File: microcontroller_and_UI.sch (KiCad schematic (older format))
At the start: 36 parts

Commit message: Annotate schematic symbols
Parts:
- gave numbers to parts that had none: 36

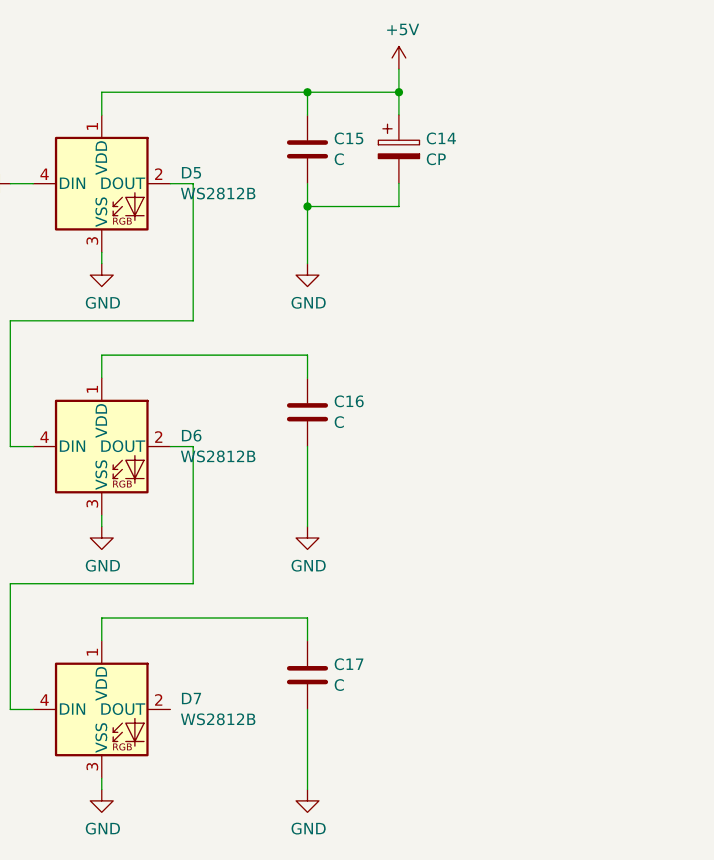
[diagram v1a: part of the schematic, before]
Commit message: Assign PCB footprints
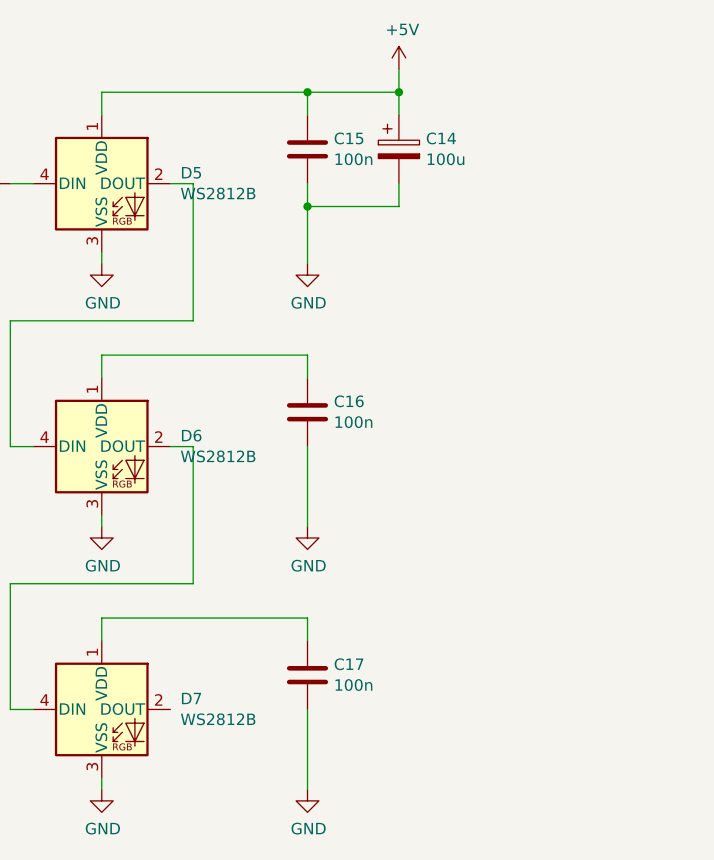
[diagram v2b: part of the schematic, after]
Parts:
- BZ1: footprint (none) -> Library:Buzzer_13.8x6.8RM7.6
- C10, C11, C12, C13, C7, C8, C9: footprint (none) -> Library:C_1206
- C14: value CP -> 100u; footprint (none) -> Library:CP_Elec_6.3x5.8
- C15, C16, C17: value C -> 100n; footprint (none) -> Library:C_1206
- C6: footprint (none) -> Library:CP_2312
- D2, D4: footprint (none) -> Library:LED_0805
- D5, D6, D7: footprint LED_SMD:LED_WS2812B_PLCC4_5.0x5.0mm_P3.2mm -> Library:LED_WS2812B
- D8: footprint (none) -> Library:D_SOD-80
- L2: footprint (none) -> Library:L_TDK_NLC453232
- Q2: footprint Package_TO_SOT_SMD:SOT-23 -> Library:SOT-23
- R10, R11, R12, R13, R14, R15, R16, R6, R7, R8, R9: footprint (none) -> Library:R_1206
- SW2, SW3: footprint (none) -> Library:SW_Push_CK_KMR2
- U3: footprint Package_QFP:TQFP-44_10x10mm_P0.8mm -> Library:TQFP-44
- Y1: footprint (none) -> Library:Crystal_HC49US
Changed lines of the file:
@@
 F 0 "U3" H 3450 3150 50  0000 C CNN
 F 1 "ATmega324PB-AU" H 3450 3050 50  0000 C CNN
-F 2 "Package_QFP:TQFP-44_10x10mm_P0.8mm" H 3900 4700 50  0001 C CIN
+F 2 "Library:TQFP-44" H 3900 4700 50  0001 C CIN
 F 3 "http://ww1.microchip.com/downloads/en/DeviceDoc/40001908A.pdf" H 3900 4700 50  0001 C CNN
 	1    3900 4700
@@
 F 0 "C7" H 1915 1496 50  0000 L CNN
 F 1 "100n" H 1915 1405 50  0000 L CNN
-F 2 "" H 1838 1300 50  0001 C CNN
+F 2 "Library:C_1206" H 1838 1300 50  0001 C CNN
 F 3 "~" H 1800 1450 50  0001 C CNN
 	1    1800 1450
@@
 F 0 "L2" H 2252 1496 50  0000 L CNN
 F 1 "10u" H 2252 1405 50  0000 L CNN
-F 2 "" H 2200 1450 50  0001 C CNN
+F 2 "Library:L_TDK_NLC453232" H 2200 1450 50  0001 C CNN
 F 3 "~" H 2200 1450 50  0001 C CNN
 	1    2200 1450
@@
 F 0 "C8" H 2315 1896 50  0000 L CNN
 F 1 "100n" H 2315 1805 50  0000 L CNN
-F 2 "" H 2238 1700 50  0001 C CNN
+F 2 "Library:C_1206" H 2238 1700 50  0001 C CNN
 F 3 "~" H 2200 1850 50  0001 C CNN
 	1    2200 1850
@@
 F 0 "C6" H 1518 1496 50  0000 L CNN
 F 1 "10u" H 1518 1405 50  0000 L CNN
-F 2 "" H 1438 1300 50  0001 C CNN
+F 2 "Library:CP_2312" H 1438 1300 50  0001 C CNN
 F 3 "~" H 1400 1450 50  0001 C CNN
 	1    1400 1450
@@
 F 0 "D8" V 2154 3230 50  0000 L CNN
 F 1 "D" V 2245 3230 50  0000 L CNN
-F 2 "" H 2200 3150 50  0001 C CNN
+F 2 "Library:D_SOD-80" H 2200 3150 50  0001 C CNN
 F 3 "~" H 2200 3150 50  0001 C CNN
 	1    2200 3150
@@
 F 0 "R7" H 1870 3196 50  0000 L CNN
 F 1 "4k7" H 1870 3105 50  0000 L CNN
-F 2 "" V 1730 3150 50  0001 C CNN
+F 2 "Library:R_1206" V 1730 3150 50  0001 C CNN
 F 3 "~" H 1800 3150 50  0001 C CNN
 	1    1800 3150
@@
 F 0 "C9" H 1915 4296 50  0000 L CNN
 F 1 "100n" H 1915 4205 50  0000 L CNN
-F 2 "" H 1838 4100 50  0001 C CNN
+F 2 "Library:C_1206" H 1838 4100 50  0001 C CNN
 F 3 "~" H 1800 4250 50  0001 C CNN
 	1    1800 4250
@@
 F 0 "SW2" V 1354 3848 50  0000 L CNN
 F 1 "SW_Push" V 1445 3848 50  0000 L CNN
-F 2 "" H 1400 3900 50  0001 C CNN
+F 2 "Library:SW_Push_CK_KMR2" H 1400 3900 50  0001 C CNN
 F 3 "~" H 1400 3900 50  0001 C CNN
 	1    1400 3700
@@
 F 0 "R6" H 1470 4296 50  0000 L CNN
 F 1 "330R" H 1470 4205 50  0000 L CNN
-F 2 "" V 1330 4250 50  0001 C CNN
+F 2 "Library:R_1206" V 1330 4250 50  0001 C CNN
 F 3 "~" H 1400 4250 50  0001 C CNN
 	1    1400 4250
@@
 F 0 "C10" V 2298 4100 50  0000 C CNN
 F 1 "22p" V 2389 4100 50  0000 C CNN
-F 2 "" H 2588 3950 50  0001 C CNN
+F 2 "Library:C_1206" H 2588 3950 50  0001 C CNN
 F 3 "~" H 2550 4100 50  0001 C CNN
 	1    2550 4100
@@
 F 0 "C11" V 2298 4400 50  0000 C CNN
 F 1 "22p" V 2389 4400 50  0000 C CNN
-F 2 "" H 2588 4250 50  0001 C CNN
+F 2 "Library:C_1206" H 2588 4250 50  0001 C CNN
 F 3 "~" H 2550 4400 50  0001 C CNN
 	1    2550 4400
@@
 F 0 "Y1" V 2754 4381 50  0000 L CNN
 F 1 "Crystal" V 2845 4381 50  0000 L CNN
-F 2 "" H 2800 4250 50  0001 C CNN
+F 2 "Library:Crystal_HC49US" H 2800 4250 50  0001 C CNN
 F 3 "~" H 2800 4250 50  0001 C CNN
 	1    2800 4250
@@
 F 0 "C12" H 2665 4996 50  0000 L CNN
 F 1 "100n" H 2665 4905 50  0000 L CNN
-F 2 "" H 2588 4800 50  0001 C CNN
+F 2 "Library:C_1206" H 2588 4800 50  0001 C CNN
 F 3 "~" H 2550 4950 50  0001 C CNN
 	1    2550 4950
@@
 F 0 "R8" H 4570 1496 50  0000 L CNN
 F 1 "4k7" H 4570 1405 50  0000 L CNN
-F 2 "" V 4430 1450 50  0001 C CNN
+F 2 "Library:R_1206" V 4430 1450 50  0001 C CNN
 F 3 "~" H 4500 1450 50  0001 C CNN
 	1    4500 1450
@@
 F 0 "R9" H 4570 1896 50  0000 L CNN
 F 1 "7k5" H 4570 1805 50  0000 L CNN
-F 2 "" V 4430 1850 50  0001 C CNN
+F 2 "Library:R_1206" V 4430 1850 50  0001 C CNN
 F 3 "~" H 4500 1850 50  0001 C CNN
 	1    4500 1850
@@
 F 0 "R11" H 7120 5446 50  0000 L CNN
 F 1 "1k" H 7120 5355 50  0000 L CNN
-F 2 "" V 6980 5400 50  0001 C CNN
+F 2 "Library:R_1206" V 6980 5400 50  0001 C CNN
 F 3 "~" H 7050 5400 50  0001 C CNN
 	1    7050 5400
@@
 F 0 "R10" H 6070 5446 50  0000 L CNN
 F 1 "1k" H 6070 5355 50  0000 L CNN
-F 2 "" V 5930 5400 50  0001 C CNN
+F 2 "Library:R_1206" V 5930 5400 50  0001 C CNN
 F 3 "~" H 6000 5400 50  0001 C CNN
 	1    6000 5400
@@
 F 0 "D4" V 7089 5782 50  0000 R CNN
 F 1 "YELLOW LED" V 6998 5782 50  0000 R CNN
-F 2 "" H 7050 5900 50  0001 C CNN
+F 2 "Library:LED_0805" H 7050 5900 50  0001 C CNN
 F 3 "~" H 7050 5900 50  0001 C CNN
 	1    7050 5900
@@
 F 0 "D2" V 6039 5782 50  0000 R CNN
 F 1 "GREEN LED" V 5948 5782 50  0000 R CNN
-F 2 "" H 6000 5900 50  0001 C CNN
+F 2 "Library:LED_0805" H 6000 5900 50  0001 C CNN
 F 3 "~" H 6000 5900 50  0001 C CNN
 	1    6000 5900
@@
 F 0 "BZ1" H 9655 5690 50  0000 C CNN
 F 1 "Buzzer" H 9655 5599 50  0000 C CNN
-F 2 "" V 9625 5500 50  0001 C CNN
+F 2 "Library:Buzzer_13.8x6.8RM7.6" V 9625 5500 50  0001 C CNN
 F 3 "~" V 9625 5500 50  0001 C CNN
 	1    9650 5400
@@
 F 0 "R15" V 10043 5950 50  0000 C CNN
 F 1 "10k" V 10134 5950 50  0000 C CNN
-F 2 "" V 10180 5950 50  0001 C CNN
+F 2 "Library:R_1206" V 10180 5950 50  0001 C CNN
 F 3 "~" H 10250 5950 50  0001 C CNN
 	1    10250 5950
@@
 F 0 "R14" H 10120 5446 50  0000 L CNN
 F 1 "10k" H 10120 5355 50  0000 L CNN
-F 2 "" V 9980 5400 50  0001 C CNN
+F 2 "Library:R_1206" V 9980 5400 50  0001 C CNN
 F 3 "~" H 10050 5400 50  0001 C CNN
 	1    10050 5400
@@
 F 0 "Q2" H 10055 5996 50  0000 L CNN
 F 1 "BSS138" H 10055 5905 50  0000 L CNN
-F 2 "Package_TO_SOT_SMD:SOT-23" H 10050 5875 50  0001 L CIN
+F 2 "Library:SOT-23" H 10050 5875 50  0001 L CIN
 F 3 "https://www.onsemi.com/pub/Collateral/BSS138-D.PDF" H 9850 5950 50  0001 L CNN
 	1    9850 5950
@@
 F 0 "SW3" V 7954 6098 50  0000 L CNN
 F 1 "SW_Push" V 8045 6098 50  0000 L CNN
-F 2 "" H 8000 6150 50  0001 C CNN
+F 2 "Library:SW_Push_CK_KMR2" H 8000 6150 50  0001 C CNN
 F 3 "~" H 8000 6150 50  0001 C CNN
 	1    8000 5950
@@
 F 0 "C13" H 8915 5946 50  0000 L CNN
 F 1 "100n" H 8915 5855 50  0000 L CNN
-F 2 "" H 8838 5750 50  0001 C CNN
+F 2 "Library:C_1206" H 8838 5750 50  0001 C CNN
 F 3 "~" H 8800 5900 50  0001 C CNN
 	1    8800 5900
@@
 F 0 "R13" V 8343 5650 50  0000 C CNN
 F 1 "1k" V 8434 5650 50  0000 C CNN
-F 2 "" V 8480 5650 50  0001 C CNN
+F 2 "Library:R_1206" V 8480 5650 50  0001 C CNN
 F 3 "~" H 8550 5650 50  0001 C CNN
 	1    8550 5650
@@
 F 0 "R12" H 8070 5446 50  0000 L CNN
 F 1 "10k" H 8070 5355 50  0000 L CNN
-F 2 "" V 7930 5400 50  0001 C CNN
+F 2 "Library:R_1206" V 7930 5400 50  0001 C CNN
 F 3 "~" H 8000 5400 50  0001 C CNN
 	1    8000 5400
@@
 P 9300 1350
 F 0 "C14" H 9418 1396 50  0000 L CNN
-F 1 "CP" H 9418 1305 50  0000 L CNN
-F 2 "" H 9338 1200 50  0001 C CNN
+F 1 "100u" H 9418 1305 50  0000 L CNN
+F 2 "Library:CP_Elec_6.3x5.8" H 9338 1200 50  0001 C CNN
 F 3 "~" H 9300 1350 50  0001 C CNN
 	1    9300 1350
@@
 P 8900 1350
 F 0 "C15" H 9015 1396 50  0000 L CNN
-F 1 "C" H 9015 1305 50  0000 L CNN
-F 2 "" H 8938 1200 50  0001 C CNN
+F 1 "100n" H 9015 1305 50  0000 L CNN
+F 2 "Library:C_1206" H 8938 1200 50  0001 C CNN
 F 3 "~" H 8900 1350 50  0001 C CNN
 	1    8900 1350
@@
 P 8900 2500
 F 0 "C16" H 9015 2546 50  0000 L CNN
-F 1 "C" H 9015 2455 50  0000 L CNN
-F 2 "" H 8938 2350 50  0001 C CNN
+F 1 "100n" H 9015 2455 50  0000 L CNN
+F 2 "Library:C_1206" H 8938 2350 50  0001 C CNN
 F 3 "~" H 8900 2500 50  0001 C CNN
 	1    8900 2500
@@
 P 8900 3650
 F 0 "C17" H 9015 3696 50  0000 L CNN
-F 1 "C" H 9015 3605 50  0000 L CNN
-F 2 "" H 8938 3500 50  0001 C CNN
+F 1 "100n" H 9015 3605 50  0000 L CNN
+F 2 "Library:C_1206" H 8938 3500 50  0001 C CNN
 F 3 "~" H 8900 3650 50  0001 C CNN
 	1    8900 3650
@@
 F 0 "R16" V 7243 1500 50  0000 C CNN
 F 1 "330R" V 7334 1500 50  0000 C CNN
-F 2 "" V 7380 1500 50  0001 C CNN
+F 2 "Library:R_1206" V 7380 1500 50  0001 C CNN
 F 3 "~" H 7450 1500 50  0001 C CNN
 	1    7450 1500
@@
 F 0 "D5" H 8344 1546 50  0000 L CNN
 F 1 "WS2812B" H 8344 1455 50  0000 L CNN
-F 2 "LED_SMD:LED_WS2812B_PLCC4_5.0x5.0mm_P3.2mm" H 8050 1200 50  0001 L TNN
+F 2 "Library:LED_WS2812B" H 8050 1200 50  0001 L TNN
 F 3 "https://cdn-shop.adafruit.com/datasheets/WS2812B.pdf" H 8100 1125 50  0001 L TNN
 	1    8000 1500
@@
 F 0 "D6" H 8344 2696 50  0000 L CNN
 F 1 "WS2812B" H 8344 2605 50  0000 L CNN
-F 2 "LED_SMD:LED_WS2812B_PLCC4_5.0x5.0mm_P3.2mm" H 8050 2350 50  0001 L TNN
+F 2 "Library:LED_WS2812B" H 8050 2350 50  0001 L TNN
 F 3 "https://cdn-shop.adafruit.com/datasheets/WS2812B.pdf" H 8100 2275 50  0001 L TNN
 	1    8000 2650
@@
 F 0 "D7" H 8344 3846 50  0000 L CNN
 F 1 "WS2812B" H 8344 3755 50  0000 L CNN
-F 2 "LED_SMD:LED_WS2812B_PLCC4_5.0x5.0mm_P3.2mm" H 8050 3500 50  0001 L TNN
+F 2 "Library:LED_WS2812B" H 8050 3500 50  0001 L TNN
 F 3 "https://cdn-shop.adafruit.com/datasheets/WS2812B.pdf" H 8100 3425 50  0001 L TNN
 	1    8000 3800

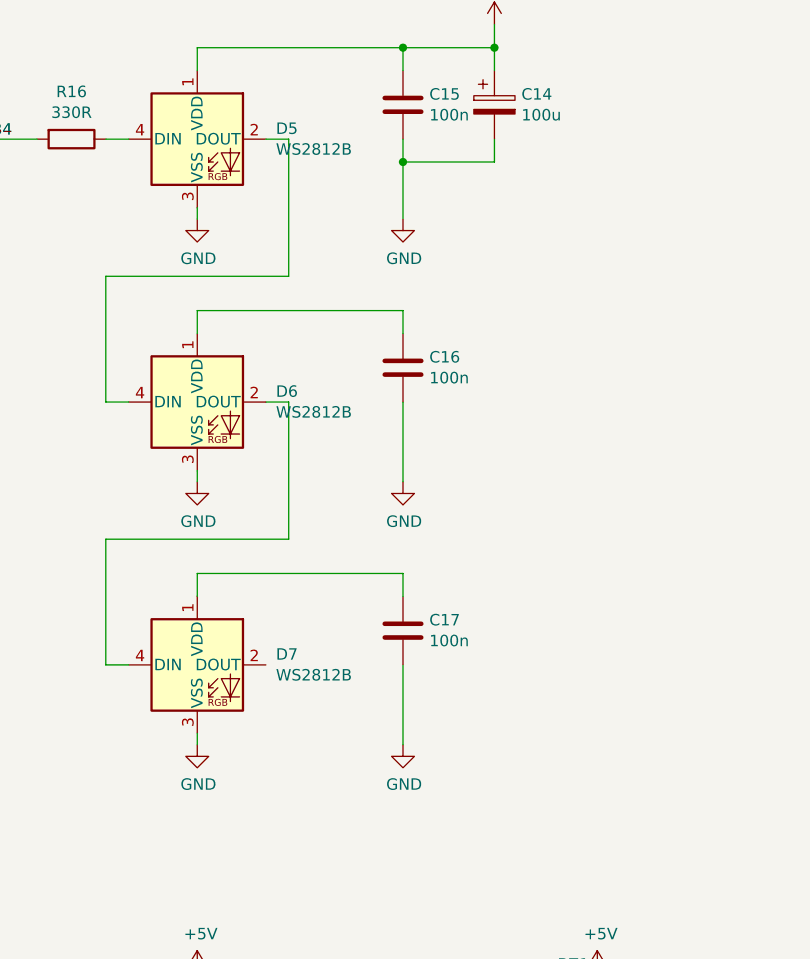
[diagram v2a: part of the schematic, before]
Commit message: Add PCB layout
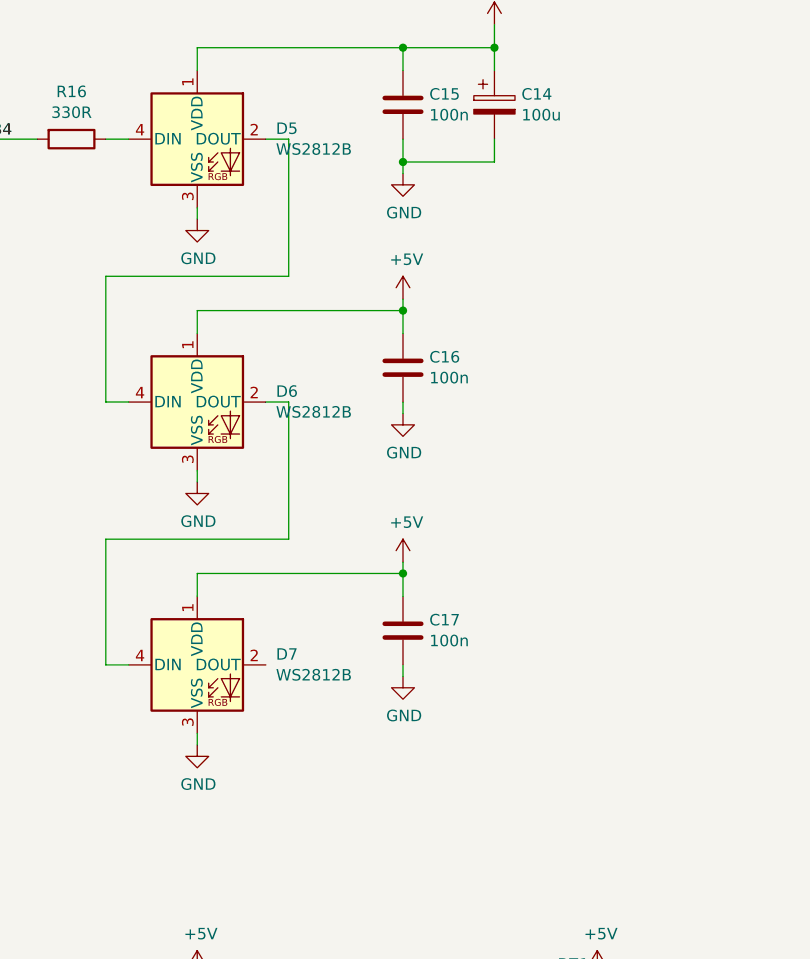
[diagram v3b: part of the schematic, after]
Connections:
- net +5V: now also C16.1, C17.1, D6.1 (VDD), D7.1 (VDD)
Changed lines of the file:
@@
 L power:GND #PWR036
 U 1 1 60D13095
-P 8900 1850
-F 0 "#PWR036" H 8900 1600 50  0001 C CNN
-F 1 "GND" H 8905 1677 50  0000 C CNN
-F 2 "" H 8900 1850 50  0001 C CNN
-F 3 "" H 8900 1850 50  0001 C CNN
-	1    8900 1850
+P 8900 1650
+F 0 "#PWR036" H 8900 1400 50  0001 C CNN
+F 1 "GND" H 8905 1477 50  0000 C CNN
+F 2 "" H 8900 1650 50  0001 C CNN
+F 3 "" H 8900 1650 50  0001 C CNN
+	1    8900 1650
 	1    0    0    -1
 $EndComp
@@
 L power:GND #PWR037
 U 1 1 60D13E04
-P 8900 3000
-F 0 "#PWR037" H 8900 2750 50  0001 C CNN
-F 1 "GND" H 8905 2827 50  0000 C CNN
-F 2 "" H 8900 3000 50  0001 C CNN
-F 3 "" H 8900 3000 50  0001 C CNN
-	1    8900 3000
+P 8900 2700
+F 0 "#PWR037" H 8900 2450 50  0001 C CNN
+F 1 "GND" H 8905 2527 50  0000 C CNN
+F 2 "" H 8900 2700 50  0001 C CNN
+F 3 "" H 8900 2700 50  0001 C CNN
+	1    8900 2700
 	1    0    0    -1
 $EndComp
@@
 L power:GND #PWR038
 U 1 1 60D14FF5
-P 8900 4150
-F 0 "#PWR038" H 8900 3900 50  0001 C CNN
-F 1 "GND" H 8905 3977 50  0000 C CNN
-F 2 "" H 8900 4150 50  0001 C CNN
-F 3 "" H 8900 4150 50  0001 C CNN
-	1    8900 4150
+P 8900 3850
+F 0 "#PWR038" H 8900 3600 50  0001 C CNN
+F 1 "GND" H 8905 3677 50  0000 C CNN
+F 2 "" H 8900 3850 50  0001 C CNN
+F 3 "" H 8900 3850 50  0001 C CNN
+	1    8900 3850
 	1    0    0    -1
 $EndComp
@@
 	8900 3400 8900 3500
 Wire Wire Line
-	8900 3800 8900 4150
-Wire Wire Line
-	8900 3000 8900 2650
-Wire Wire Line
 	8900 2350 8900 2250
 Wire Wire Line
@@
 	8000 2250 8000 2350
 Wire Wire Line
-	8900 1850 8900 1600
-Wire Wire Line
 	8900 1600 9300 1600
 Wire Wire Line
 	9300 1600 9300 1500
-Connection ~ 8900 1600
 Wire Wire Line
 	8900 1600 8900 1500
@@
 Wire Wire Line
 	7600 1500 7700 1500
+$Comp
+L power:+5V #PWR0101
+U 1 1 60E677C7
+P 8900 2200
+F 0 "#PWR0101" H 8900 2050 50  0001 C CNN
+F 1 "+5V" H 8915 2373 50  0000 C CNN
+F 2 "" H 8900 2200 50  0001 C CNN
+F 3 "" H 8900 2200 50  0001 C CNN
+	1    8900 2200
+	1    0    0    -1
+$EndComp
+$Comp
+L power:+5V #PWR0102
+U 1 1 60E80E24
+P 8900 3350
+F 0 "#PWR0102" H 8900 3200 50  0001 C CNN
+F 1 "+5V" H 8915 3523 50  0000 C CNN
+F 2 "" H 8900 3350 50  0001 C CNN
+F 3 "" H 8900 3350 50  0001 C CNN
+	1    8900 3350
+	1    0    0    -1
+$EndComp
+Wire Wire Line
+	8900 1650 8900 1600
+Connection ~ 8900 1600
+Wire Wire Line
+	8900 2200 8900 2250
+Connection ~ 8900 2250
+Wire Wire Line
+	8900 2700 8900 2650
+Wire Wire Line
+	8900 3400 8900 3350
+Connection ~ 8900 3400
+Wire Wire Line
+	8900 3850 8900 3800
 $EndSCHEMATC

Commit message: Update and rename files
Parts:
- SW2, SW3: footprint Library:SW_Push_CK_KMR2 -> Library:SW_Push_SCHURTER_1301.9319
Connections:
- net +BATT renamed +VSW
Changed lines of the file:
@@
 F 0 "SW2" V 1354 3848 50  0000 L CNN
 F 1 "SW_Push" V 1445 3848 50  0000 L CNN
-F 2 "Library:SW_Push_CK_KMR2" H 1400 3900 50  0001 C CNN
+F 2 "Library:SW_Push_SCHURTER_1301.9319" H 1400 3900 50  0001 C CNN
 F 3 "~" H 1400 3900 50  0001 C CNN
 	1    1400 3700
@@
 	1    0    0    -1
 $EndComp
-$Comp
-L power:+BATT #PWR026
-U 1 1 60BF2A59
-P 4500 1000
-F 0 "#PWR026" H 4500 850 50  0001 C CNN
-F 1 "+BATT" H 4515 1173 50  0000 C CNN
-F 2 "" H 4500 1000 50  0001 C CNN
-F 3 "" H 4500 1000 50  0001 C CNN
-	1    4500 1000
-	1    0    0    -1
-$EndComp
 Wire Wire Line
 	4500 1000 4500 1300
@@
 F 0 "SW3" V 7954 6098 50  0000 L CNN
 F 1 "SW_Push" V 8045 6098 50  0000 L CNN
-F 2 "Library:SW_Push_CK_KMR2" H 8000 6150 50  0001 C CNN
+F 2 "Library:SW_Push_SCHURTER_1301.9319" H 8000 6150 50  0001 C CNN
 F 3 "~" H 8000 6150 50  0001 C CNN
 	1    8000 5950
@@
 Wire Wire Line
 	8900 3850 8900 3800
+$Comp
+L power:+VSW #PWR?
+U 1 1 60F1BFD3
+P 4500 1000
+F 0 "#PWR?" H 4500 850 50  0001 C CNN
+F 1 "+VSW" H 4515 1173 50  0000 C CNN
+F 2 "" H 4500 1000 50  0001 C CNN
+F 3 "" H 4500 1000 50  0001 C CNN
+	1    4500 1000
+	1    0    0    -1
+$EndComp
 $EndSCHEMATC

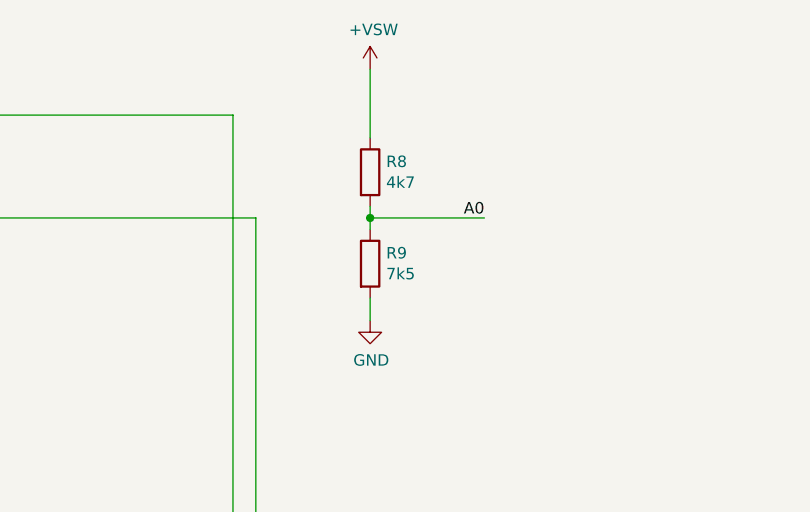
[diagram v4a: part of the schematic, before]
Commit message: Change R8 and R9 values
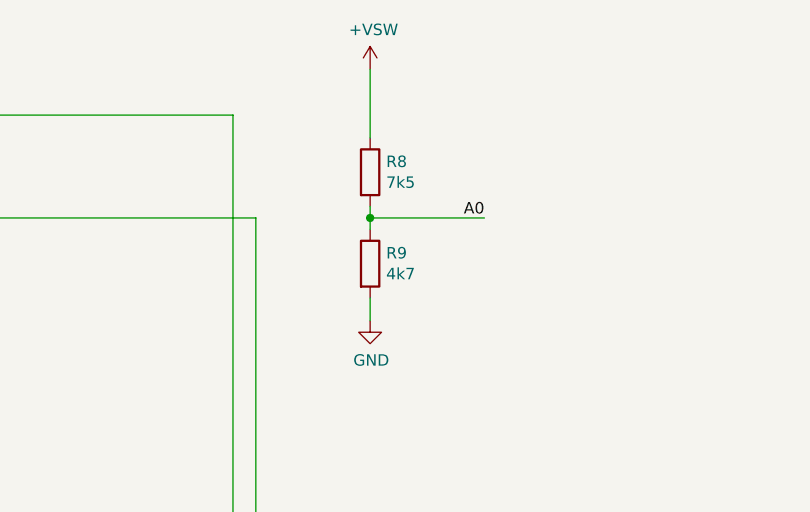
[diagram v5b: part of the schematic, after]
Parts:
- R8: value 4k7 -> 7k5
- R9: value 7k5 -> 4k7
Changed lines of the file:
@@
 P 4500 1450
 F 0 "R8" H 4570 1496 50  0000 L CNN
-F 1 "4k7" H 4570 1405 50  0000 L CNN
+F 1 "7k5" H 4570 1405 50  0000 L CNN
 F 2 "Library:R_1206" V 4430 1450 50  0001 C CNN
 F 3 "~" H 4500 1450 50  0001 C CNN
@@
 P 4500 1850
 F 0 "R9" H 4570 1896 50  0000 L CNN
-F 1 "7k5" H 4570 1805 50  0000 L CNN
+F 1 "4k7" H 4570 1805 50  0000 L CNN
 F 2 "Library:R_1206" V 4430 1850 50  0001 C CNN
 F 3 "~" H 4500 1850 50  0001 C CNN
